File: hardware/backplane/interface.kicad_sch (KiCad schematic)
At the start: 5 parts, among them J2 FR_1,27/80-xx, J3 SFH11-PBPC-D13-RA-BK, J4 FR_1,27/80-xx

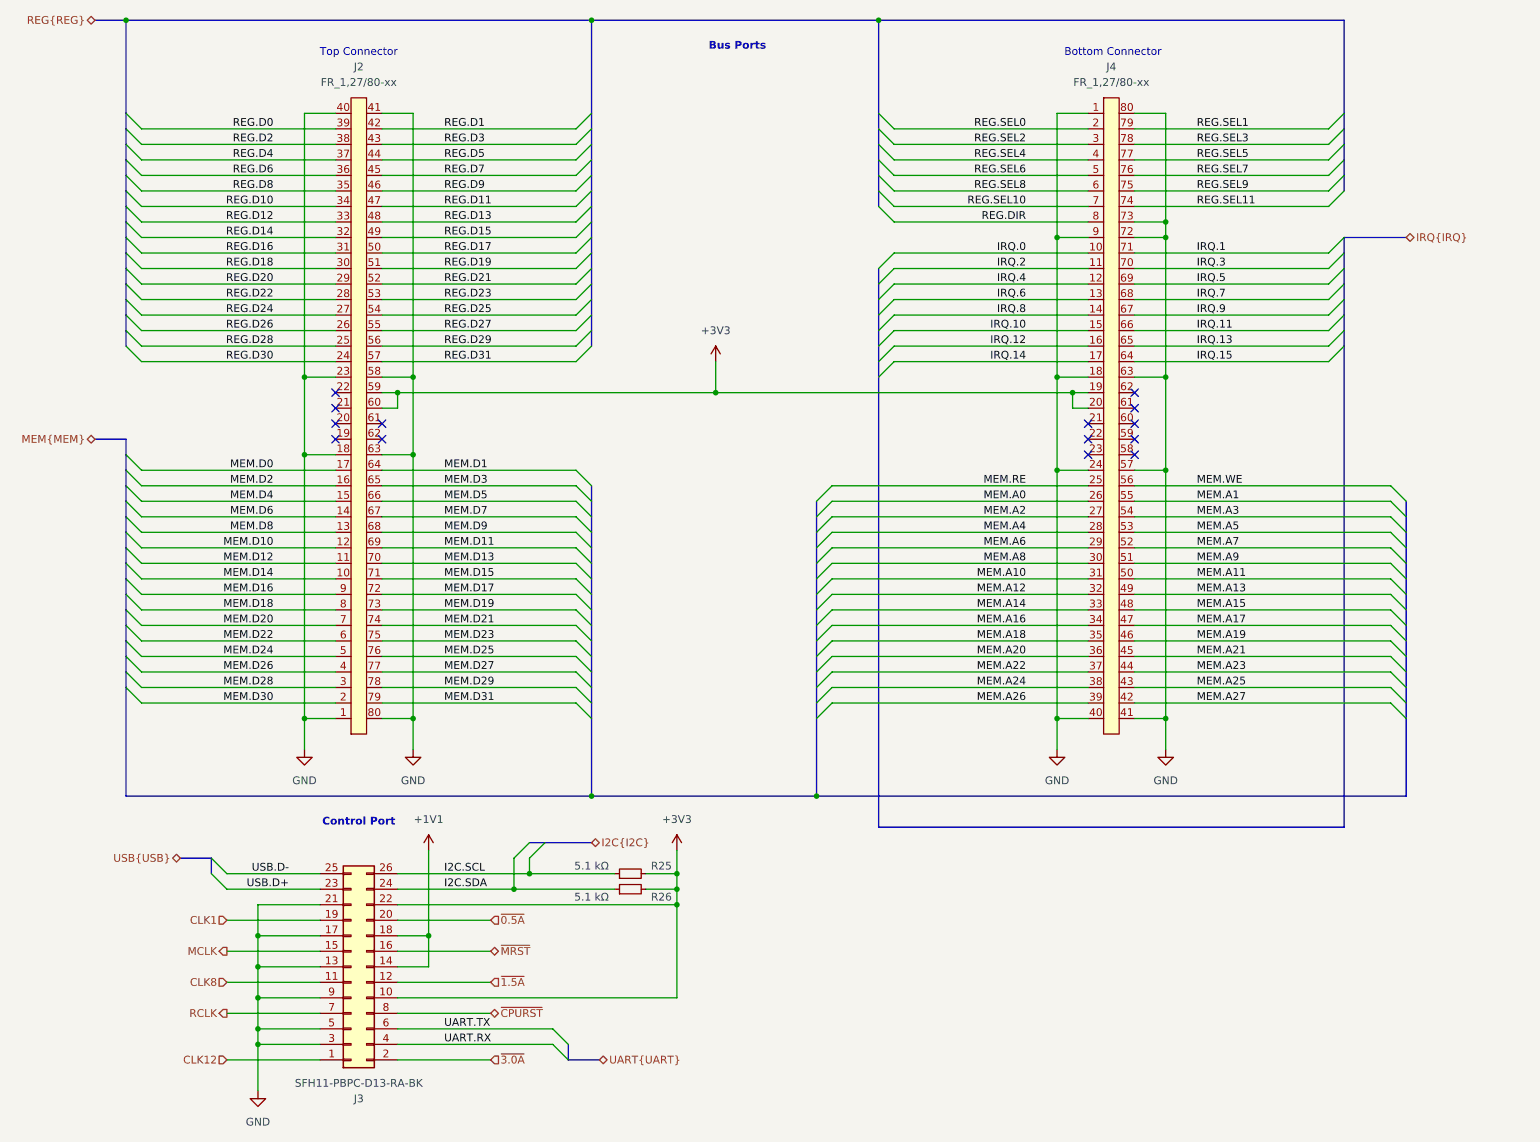
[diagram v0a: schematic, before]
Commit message: feat: Re-add peripheral MCLK, add to memory lines (#3)
Need MCLK to maintain peripheral synchronization.  Add missing memory
access size and latch lines.
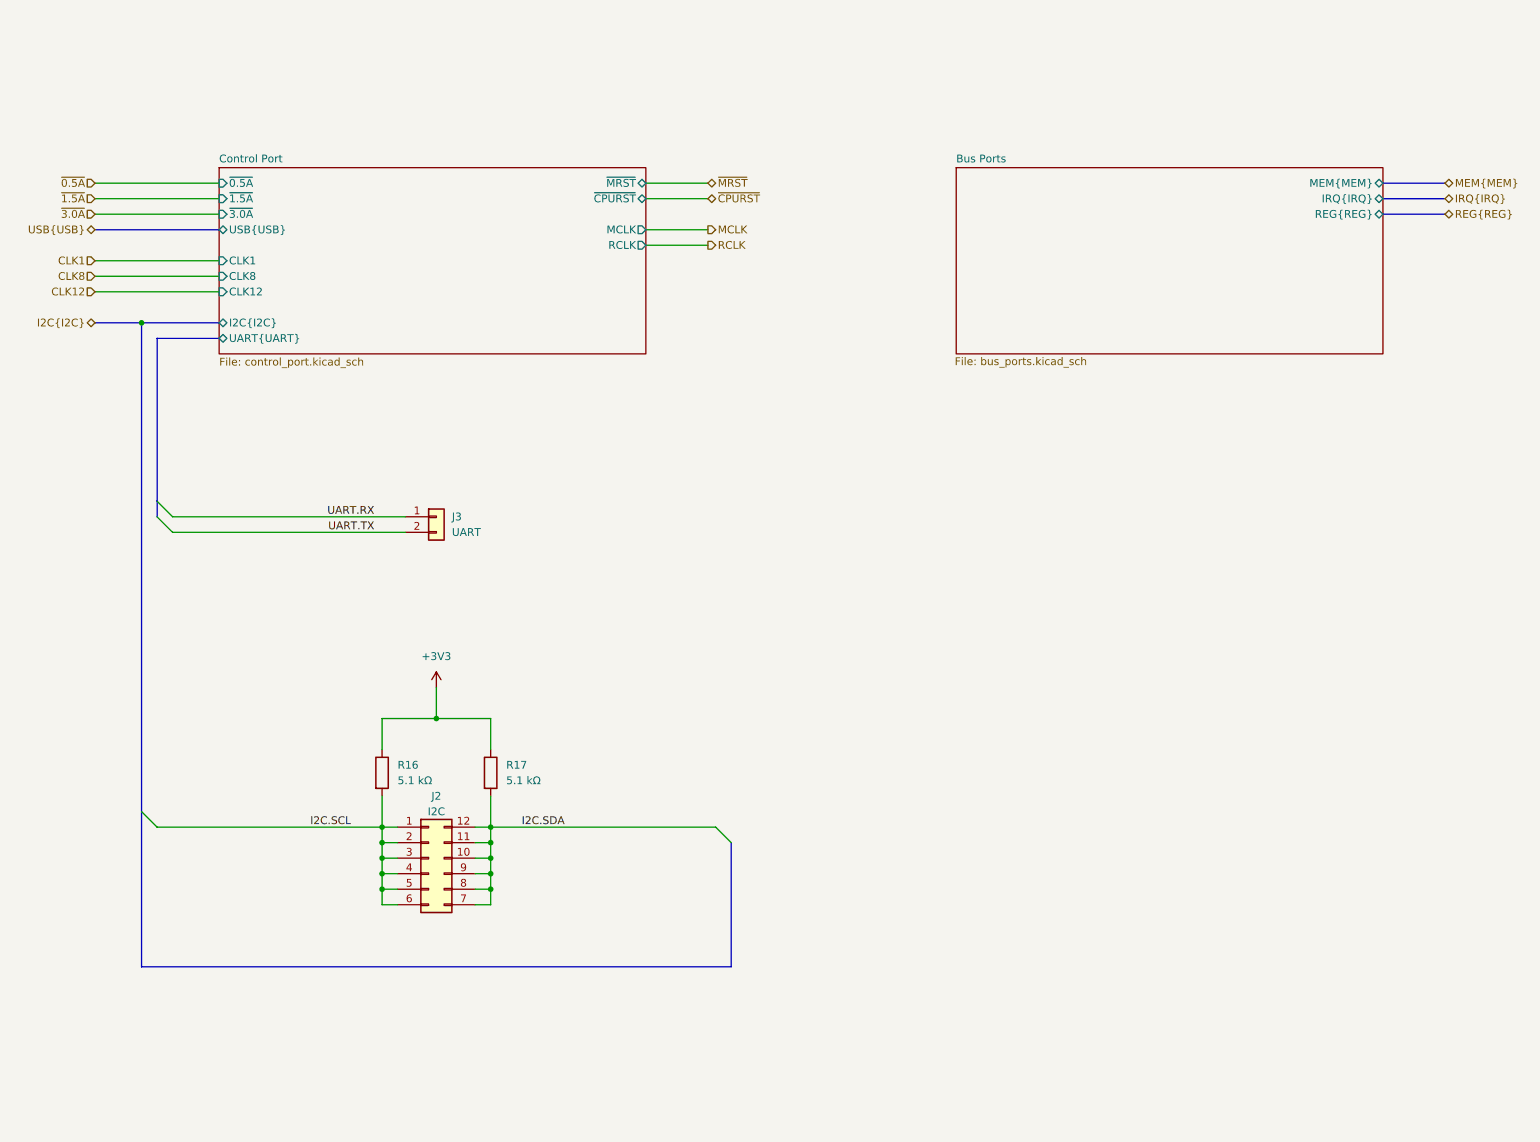
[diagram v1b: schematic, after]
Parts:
- removed J2, J4: FR_1,27/80-xx, symbol FR-1-27-80-xx:FR_1,27/80-xx
- removed J3: SFH11-PBPC-D13-RA-BK, Connector_PinSocket_2.54mm:PinSocket_2x13_P2.54mm_Horizontal, symbol Connector_Generic:Conn_02x13_Odd_Even
- removed R25, R26: 5.1 kΩ, symbol Device:R_Small
- added J2: I2C, symbol Connector_Generic:Conn_02x06_Counter_Clockwise
- added J3: UART, symbol Connector_Generic:Conn_01x02
- added R16, R17: 5.1 kΩ, symbol Device:R
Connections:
- net +3V3: now also R16.1, R17.1
- net I2C.SCL: now also J2.1 (Pin_1), J2.2 (Pin_2), J2.3 (Pin_3), J2.4 (Pin_4), J2.5 (Pin_5), J2.6 (Pin_6), R16.2
- net I2C.SDA: now also J2.10 (Pin_10), J2.11 (Pin_11), J2.12 (Pin_12), J2.7 (Pin_7), J2.8 (Pin_8), J2.9 (Pin_9), R17.2
- net UART.RX: now also J3.1 (Pin_1)
- net UART.TX: now also J3.2 (Pin_2)
- no-connect marks 14 -> 0
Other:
- added sheet Bus Ports (bus_ports.kicad_sch)
- added sheet Control Port (control_port.kicad_sch)
- note removed: "Bottom Connector"
- note removed: "Bus Ports"
- note removed: "Control Port"
- note removed: "Top Connector"
- title: RVFS Access Port -> RVFS External Interface

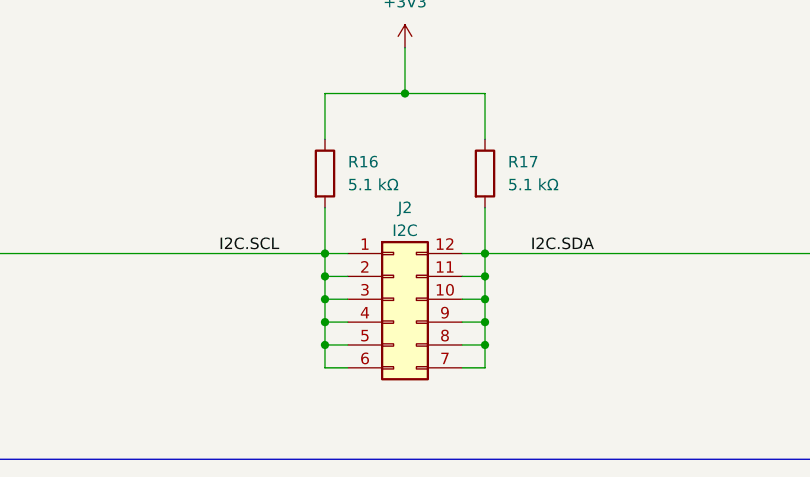
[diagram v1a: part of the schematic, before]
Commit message: feat: Assign footprints, add testpoints
 * Verify all footprints are assigned.
 * Create testpoints for key signals.
 * Reorganize component libraries.
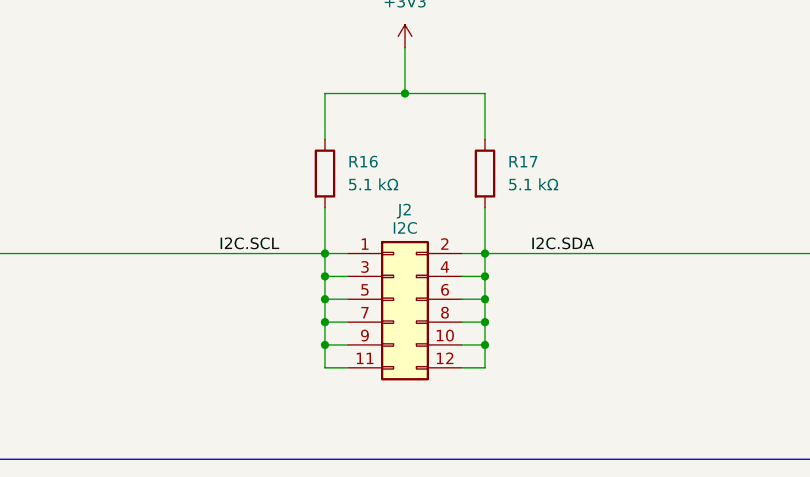
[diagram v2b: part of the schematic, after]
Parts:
- removed J2: I2C, symbol Connector_Generic:Conn_02x06_Counter_Clockwise
- added J2: I2C, Connector_PinHeader_2.54mm:PinHeader_2x06_P2.54mm_Vertical, symbol Connector_Generic:Conn_02x06_Odd_Even
- J3: footprint (none) -> Connector_PinHeader_2.54mm:PinHeader_1x02_P2.54mm_Vertical; Part Number (none) -> 929647-01-02-EU
- R16, R17: footprint (none) -> Resistor_SMD:R_0402_1005Metric; Part Number (none) -> CR0402-FX-5101GLF
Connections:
- net I2C.SCL: now also J2.1 (Pin_1), J2.11 (Pin_11), J2.3 (Pin_3), J2.5 (Pin_5), J2.7 (Pin_7), J2.9 (Pin_9)
- net I2C.SDA: now also J2.10 (Pin_10), J2.12 (Pin_12), J2.2 (Pin_2), J2.4 (Pin_4), J2.6 (Pin_6), J2.8 (Pin_8)
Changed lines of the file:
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@@
 			)
 		)
-		(property "Footprint" ""
-			(at 93.98 96.52 0)
-			(effects
-				(font
-					(size 1.27 1.27)
-				)
-				(hide yes)
-			)
-		)
-		(property "Datasheet" "~"
+		(property "Footprint" "Connector_PinHeader_2.54mm:PinHeader_1x02_P2.54mm_Vertical"
+			(at 93.98 96.52 0)
+			(effects
+				(font
+					(size 1.27 1.27)
+				)
+				(hide yes)
+			)
+		)
+		(property "Datasheet" "https://multimedia.3m.com/mws/media/43897O/3mtmpinstriphdr-100-100x-100-929-series-ts0769.pdf"
 			(at 93.98 96.52 0)
 			(effects
@@
 		)
 		(property "Description" "Generic connector, single row, 01x02, script generated (kicad-library-utils/schlib/autogen/connector/)"
+			(at 93.98 96.52 0)
+			(effects
+				(font
+					(size 1.27 1.27)
+				)
+				(hide yes)
+			)
+		)
+		(property "Indicates" ""
+			(at 93.98 96.52 0)
+			(effects
+				(font
+					(size 1.27 1.27)
+				)
+				(hide yes)
+			)
+		)
+		(property "Part Number" "929647-01-02-EU"
 			(at 93.98 96.52 0)
 			(effects
@@
 	)
 	(symbol
+		(lib_id "Connector_Generic:Conn_02x06_Odd_Even")
+		(at 92.71 152.4 0)
+		(unit 1)
+		(exclude_from_sim no)
+		(in_bom yes)
+		(on_board yes)
+		(dnp no)
+		(property "Reference" "J2"
+			(at 93.98 142.494 0)
+			(effects
+				(font
+					(size 1.27 1.27)
+				)
+			)
+		)
+		(property "Value" "I2C"
+			(at 93.98 144.526 0)
+			(effects
+				(font
+					(size 1.27 1.27)
+				)
+			)
+		)
+		(property "Footprint" "Connector_PinHeader_2.54mm:PinHeader_2x06_P2.54mm_Vertical"
+			(at 92.71 152.4 0)
+			(effects
+				(font
+					(size 1.27 1.27)
+				)
+				(hide yes)
+			)
+		)
+		(property "Datasheet" "https://app.adam-tech.com/products/download/data_sheet/202065/ph2-xx-ua-data-sheet.pdf"
+			(at 92.71 152.4 0)
+			(effects
+				(font
+					(size 1.27 1.27)
+				)
+				(hide yes)
+			)
+		)
+		(property "Description" "Generic connector, double row, 02x06, odd/even pin numbering scheme (row 1 odd numbers, row 2 even numbers), script generated (kicad-library-utils/schlib/autogen/connector/)"
+			(at 92.71 152.4 0)
+			(effects
+				(font
+					(size 1.27 1.27)
+				)
+				(hide yes)
+			)
+		)
+		(property "Indicates" ""
+			(at 92.71 152.4 0)
+			(effects
+				(font
+					(size 1.27 1.27)
+				)
+				(hide yes)
+			)
+		)
+		(property "Part Number" "PH2-12-UA"
+			(at 92.71 152.4 0)
+			(effects
+				(font
+					(size 1.27 1.27)
+				)
+				(hide yes)
+			)
+		)
+		(pin "6"
+		)
+		(pin "8"
+		)
+		(pin "1"
+		)
+		(pin "7"
+		)
+		(pin "2"
+		)
+		(pin "9"
+		)
+		(pin "12"
+		)
+		(pin "5"
+		)
+		(pin "11"
+		)
+		(pin "4"
+		)
+		(pin "10"
+		)
+		(pin "3"
+		)
+		(instances
+			(project ""
+				(path "/b4bde1b3-859c-4538-a8f1-0c6fb216a957/bd7ce088-b816-4c7b-96cf-5c9cefb5e628"
+					(reference "J2")
+					(unit 1)
+				)
+			)
+		)
+	)
+	(symbol
 		(lib_id "Device:R")
 		(at 85.09 138.43 0)
@@
 			)
 		)
-		(property "Footprint" ""
+		(property "Footprint" "Resistor_SMD:R_0402_1005Metric"
 			(at 83.312 138.43 90)
 			(effects
@@
 			)
 		)
-		(property "Datasheet" "~"
+		(property "Datasheet" "https://www.bourns.com/docs/product-datasheets/cr.pdf?sfvrsn=574d41f6_14"
 			(at 85.09 138.43 0)
 			(effects
@@
 		)
 		(property "Description" "Resistor"
+			(at 85.09 138.43 0)
+			(effects
+				(font
+					(size 1.27 1.27)
+				)
+				(hide yes)
+			)
+		)
+		(property "Indicates" ""
+			(at 85.09 138.43 0)
+			(effects
+				(font
+					(size 1.27 1.27)
+				)
+				(hide yes)
+			)
+		)
+		(property "Part Number" "CR0402-FX-5101GLF"
 			(at 85.09 138.43 0)
 			(effects
@@
 				(path "/b4bde1b3-859c-4538-a8f1-0c6fb216a957/bd7ce088-b816-4c7b-96cf-5c9cefb5e628"
 					(reference "R16")
-					(unit 1)
-				)
-			)
-		)
-	)
-	(symbol
-		(lib_id "Connector_Generic:Conn_02x06_Counter_Clockwise")
-		(at 92.71 152.4 0)
-		(unit 1)
-		(exclude_from_sim no)
-		(in_bom yes)
-		(on_board yes)
-		(dnp no)
-		(property "Reference" "J2"
-			(at 93.98 142.24 0)
-			(effects
-				(font
-					(size 1.27 1.27)
-				)
-			)
-		)
-		(property "Value" "I2C"
-			(at 93.98 144.78 0)
-			(effects
-				(font
-					(size 1.27 1.27)
-				)
-			)
-		)
-		(property "Footprint" ""
-			(at 92.71 152.4 0)
-			(effects
-				(font
-					(size 1.27 1.27)
-				)
-				(hide yes)
-			)
-		)
-		(property "Datasheet" "~"
-			(at 92.71 152.4 0)
-			(effects
-				(font
-					(size 1.27 1.27)
-				)
-				(hide yes)
-			)
-		)
-		(property "Description" "Generic connector, double row, 02x06, counter clockwise pin numbering scheme (similar to DIP package numbering), script generated (kicad-library-utils/schlib/autogen/connector/)"
-			(at 92.71 152.4 0)
-			(effects
-				(font
-					(size 1.27 1.27)
-				)
-				(hide yes)
-			)
-		)
-		(pin "7"
-		)
-		(pin "8"
-		)
-		(pin "1"
-		)
-		(pin "6"
-		)
-		(pin "2"
-		)
-		(pin "9"
-		)
-		(pin "4"
-		)
-		(pin "3"
-		)
-		(pin "12"
-		)
-		(pin "10"
-		)
-		(pin "11"
-		)
-		(pin "5"
-		)
-		(instances
-			(project ""
-				(path "/b4bde1b3-859c-4538-a8f1-0c6fb216a957/bd7ce088-b816-4c7b-96cf-5c9cefb5e628"
-					(reference "J2")
 					(unit 1)
 				)
@@
 			)
 		)
-		(property "Footprint" ""
+		(property "Footprint" "Resistor_SMD:R_0402_1005Metric"
 			(at 101.092 138.43 90)
 			(effects
@@
 			)
 		)
-		(property "Datasheet" "~"
+		(property "Datasheet" "https://www.bourns.com/docs/product-datasheets/cr.pdf?sfvrsn=574d41f6_14"
 			(at 102.87 138.43 0)
 			(effects
@@
 			(at 102.87 138.43 0)
 			(effects
+				(font
+					(size 1.27 1.27)
+				)
+				(hide yes)
+			)
+		)
+		(property "Indicates" ""
+			(at 102.87 138.43 0)
+			(effects
+				(font
+					(size 1.27 1.27)
+				)
+				(hide yes)
+			)
+		)
+		(property "Part Number" "CR0402-FX-5101GLF"
+			(at 102.87 138.43 0)
+			(effects

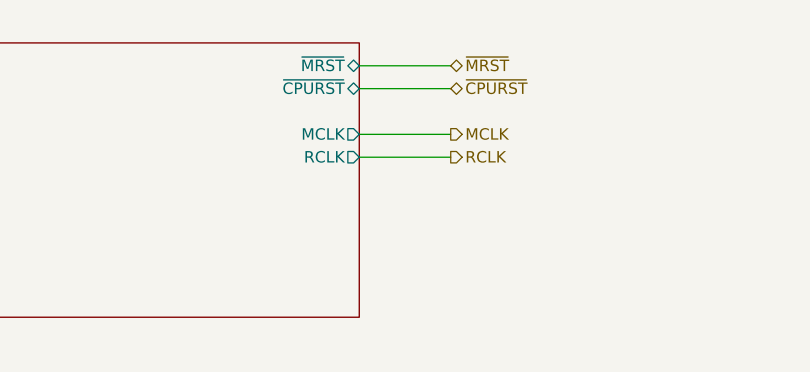
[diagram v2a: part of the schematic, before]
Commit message: feat: Apply bus arch changes to backplane schematic
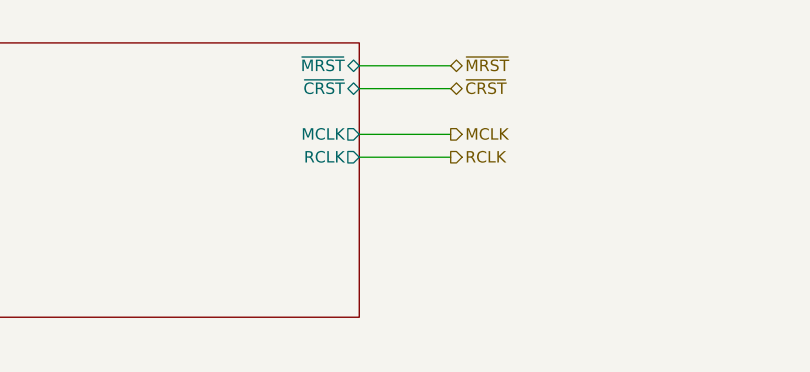
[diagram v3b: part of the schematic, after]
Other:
- sheet Control Port ports: added ~{CRST}; removed ~{CPURST}
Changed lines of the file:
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@@
 		)
 	)
-	(hierarchical_label "~{CPURST}"
+	(hierarchical_label "~{CRST}"
 		(shape bidirectional)
 		(at 138.43 44.45 0)
@@
 			)
 		)
-		(pin "~{CPURST}" bidirectional
+		(pin "~{CRST}" bidirectional
 			(at 128.27 44.45 0)
 			(effects
